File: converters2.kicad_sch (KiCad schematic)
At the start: 28 parts, among them U11 MCP4728, U12 TLV3502AIDR, U13 TLV3502AIDR, U14 MCP4728, U15 TLV3502AIDR, U16 TLV3502AIDR, U17 MCP4728, U18 TLV3502AIDR, U19 TLV3502AIDR

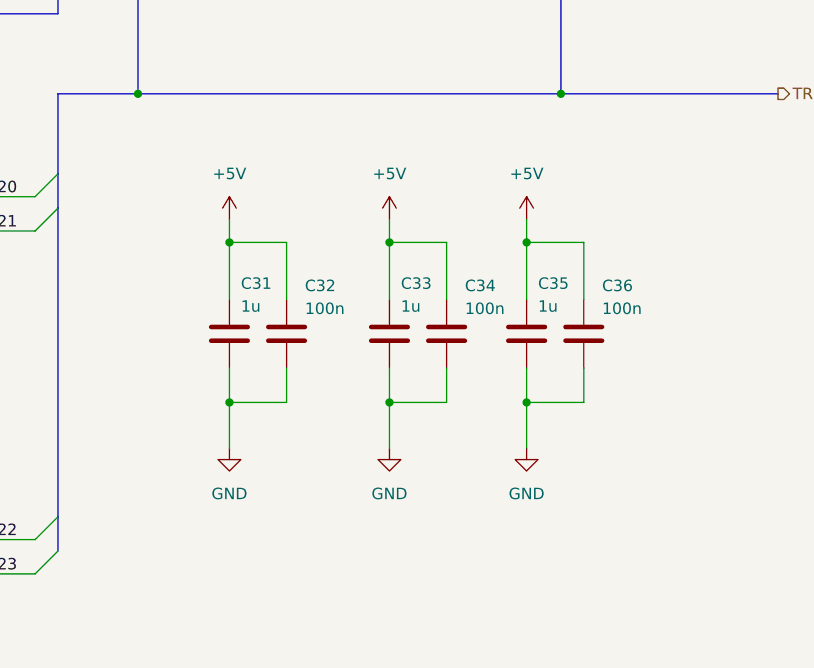
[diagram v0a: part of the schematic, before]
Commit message: Added SD card readers and USB-C for power in.
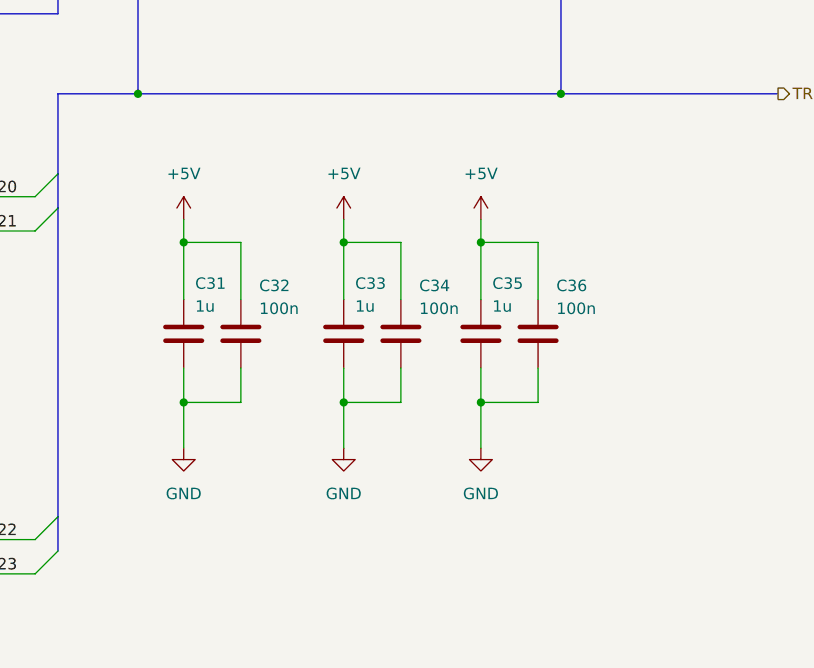
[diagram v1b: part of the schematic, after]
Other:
- moved on the sheet: C31, C32, C33, C34, C35, C36
